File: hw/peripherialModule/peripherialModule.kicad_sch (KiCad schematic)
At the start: 20 parts, among them IC1 ATA6561-GAQW-N, J1 Conn_01x13_Socket, J2 Conn_01x13_Socket, J3 G17C0900132EU, J4 G17C0900132EU, J5 Conn_01x03_Socket, J6 726386-2, J7 726386-2, SW1 SW_Push, U1 TLV76133DCYR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

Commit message: boards are changing
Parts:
- removed J2: Conn_01x13_Socket, Connector_PinSocket_2.54mm:PinSocket_1x13_P2.54mm_Vertical, symbol Connector:Conn_01x13_Socket
- removed J6, J7: 726386-2, 726386-2, symbol FASTON:726386-2
- added J6, J9: Conn_01x03_Socket, Connector_PinSocket_2.54mm:PinSocket_1x03_P2.54mm_Vertical, symbol Connector:Conn_01x03_Socket
- added J8: Conn_01x05_Socket, Connector_PinSocket_2.54mm:PinSocket_1x05_P2.54mm_Vertical, symbol Connector:Conn_01x05_Socket
- J1: value Conn_01x13_Socket -> Conn_02x11_Socket; footprint Connector_PinSocket_2.54mm:PinSocket_1x13_P2.54mm_Vertical -> Connector_PinSocket_2.54mm:PinSocket_2x11_P2.54mm_Vertical; symbol Connector:Conn_01x13_Socket -> Connector_Generic:Conn_02x11_Odd_Even
- R2: value 100 -> 1k
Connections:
- net 24V: now also J9.1 (Pin_1), J9.2 (Pin_2), J9.3 (Pin_3)
- net 5.2V: now also J1.3 (Pin_3), J1.4 (Pin_4); no longer J1.1 (Pin_1), J1.2 (Pin_2)
- net GND: now also J1.1 (Pin_1), J1.2 (Pin_2), J6.1 (Pin_1), J6.2 (Pin_2), J6.3 (Pin_3), J8.3 (Pin_3); no longer J1.3 (Pin_3)
- net ICSP_CLK: now also J8.5 (Pin_5)
- net ICSP_DAT: now also J8.4 (Pin_4)
- net RA0: now also J1.8 (Pin_8); no longer J1.6 (Pin_6)
- net RA1: now also J1.10 (Pin_10); no longer J1.7 (Pin_7)
- net RA2: now also J1.12 (Pin_12); no longer J1.8 (Pin_8)
- net RA3: now also J1.14 (Pin_14); no longer J1.9 (Pin_9)
- net RA4: now also J1.16 (Pin_16); no longer J1.10 (Pin_10)
- net RA5: now also J1.18 (Pin_18); no longer J1.11 (Pin_11)
- net RA6: now also J1.20 (Pin_20); no longer J1.12 (Pin_12)
- net RA7: now also J1.22 (Pin_22); no longer J1.13 (Pin_13)
- net RC0: now also J1.15 (Pin_15)
- net RC1: now also J1.17 (Pin_17)
- net RC2: now also J1.19 (Pin_19)
- net RC3: now also J1.21 (Pin_21)
- net RC4: now also J1.13 (Pin_13)
- net RC5: now also J1.11 (Pin_11)
- net RC6: now also J1.9 (Pin_9)
- net RC7: now also J1.7 (Pin_7)
- net VDD: now also J1.6 (Pin_6), J8.2 (Pin_2); no longer J1.4 (Pin_4)
- net ~{MCLR}: now also J8.1 (Pin_1)

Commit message: hw - ledBoard
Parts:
- C4, C6: value 0.1u -> 0.1uF
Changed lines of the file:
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@@
       (effects (font (size 1.27 1.27)) (justify left))
     )
-    (property "Value" "0.1u" (at 194.31 132.08 0)
+    (property "Value" "0.1uF" (at 194.31 132.08 0)
       (effects (font (size 1.27 1.27)) (justify left))
     )
@@
       (effects (font (size 1.27 1.27)) (justify left))
     )
-    (property "Value" "0.1u" (at 273.05 90.17 0)
-      (effects (font (size 1.27 1.27)) (justify left))
-    )
+    (property "Value" "0.1uF" (at 273.05 90.17 0)
+      (effects (font (size 1.27 1.27)) (justify left))
+    )

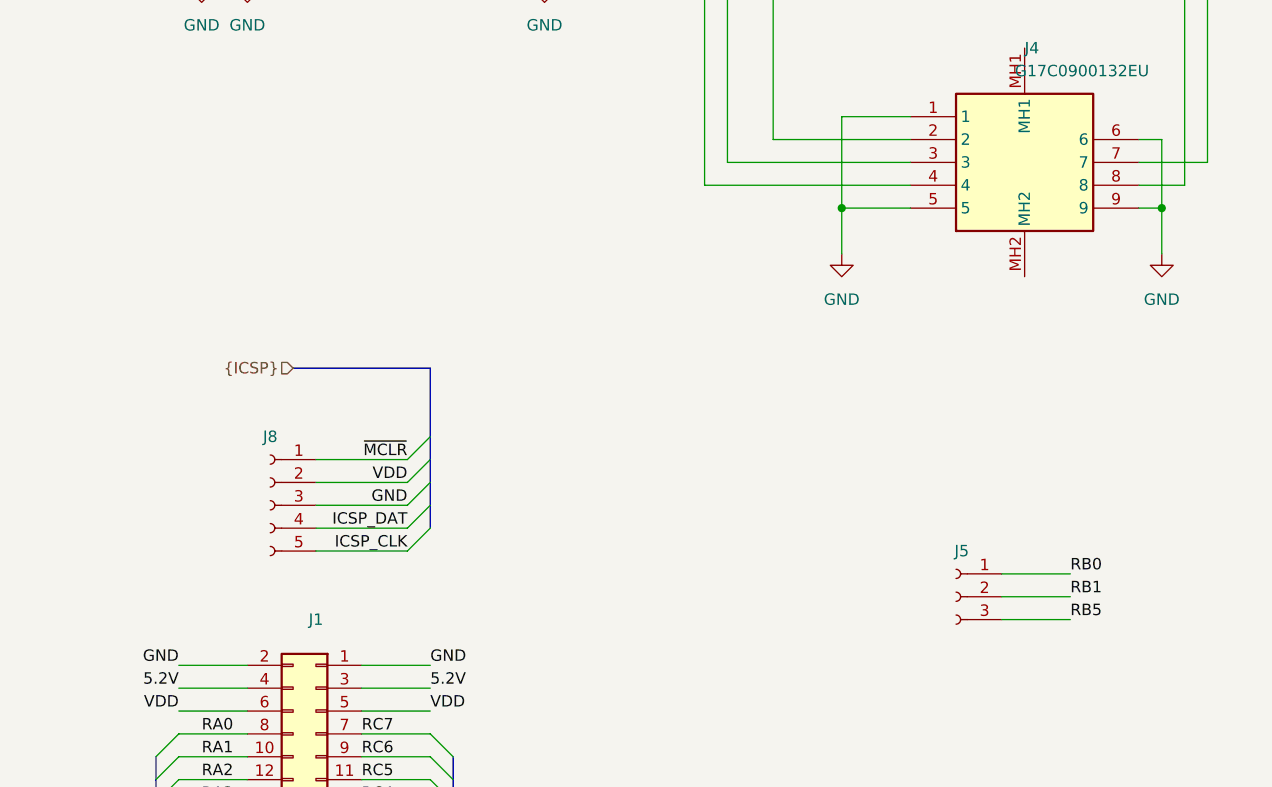
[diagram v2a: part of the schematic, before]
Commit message: text - periferie, obrazky hw - schemata
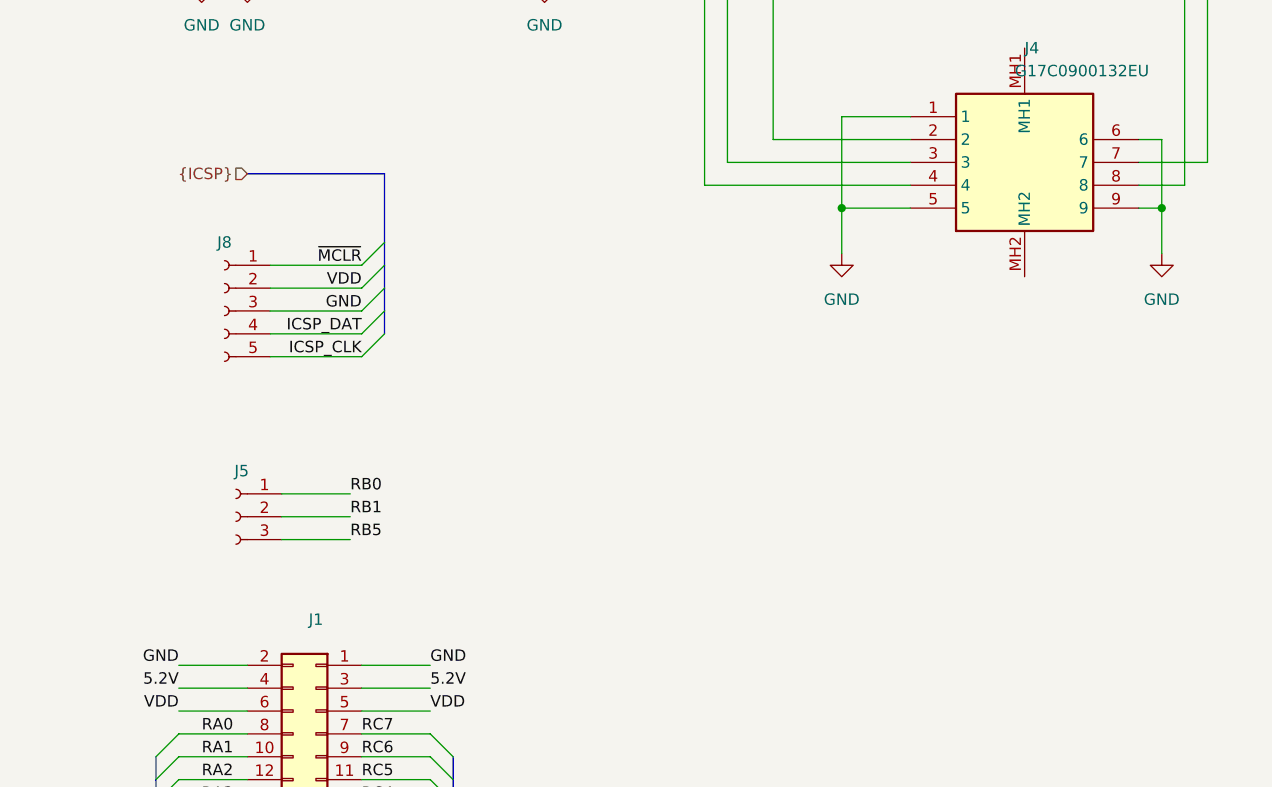
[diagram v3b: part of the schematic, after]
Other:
- moved on the sheet: J5, J8
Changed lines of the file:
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@@
     (stroke (width 0) (type default))
   )
-  (bus_entry (at 66.04 127) (size -2.54 2.54)
+  (bus_entry (at 60.96 105.41) (size -2.54 2.54)
     (stroke (width 0) (type default))
   )
@@
     (stroke (width 0) (type default))
   )
-  (bus_entry (at 66.04 137.16) (size -2.54 2.54)
+  (bus_entry (at 60.96 115.57) (size -2.54 2.54)
     (stroke (width 0) (type default))
   )
@@
     (stroke (width 0) (type default))
   )
-  (bus_entry (at 66.04 129.54) (size -2.54 2.54)
+  (bus_entry (at 60.96 107.95) (size -2.54 2.54)
     (stroke (width 0) (type default))
   )
@@
     (stroke (width 0) (type default))
   )
-  (bus_entry (at 66.04 134.62) (size -2.54 2.54)
+  (bus_entry (at 60.96 113.03) (size -2.54 2.54)
     (stroke (width 0) (type default))
   )
@@
     (stroke (width 0) (type default))
   )
-  (bus_entry (at 66.04 132.08) (size -2.54 2.54)
+  (bus_entry (at 60.96 110.49) (size -2.54 2.54)
     (stroke (width 0) (type default))
   )
@@
     (stroke (width 0) (type default))
   )
-  (wire (pts (xy 129.54 142.24) (xy 137.16 142.24))
+  (wire (pts (xy 49.53 133.35) (xy 57.15 133.35))
     (stroke (width 0) (type default))
   )
@@
     (stroke (width 0) (type default))
   )
-  (wire (pts (xy 63.5 139.7) (xy 53.34 139.7))
+  (wire (pts (xy 58.42 118.11) (xy 48.26 118.11))
     (stroke (width 0) (type default))
   )
@@
     (stroke (width 0) (type default))
   )
-  (bus (pts (xy 66.04 119.38) (xy 50.8 119.38))
+  (bus (pts (xy 60.96 97.79) (xy 45.72 97.79))
     (stroke (width 0) (type default))
   )
@@
     (stroke (width 0) (type default))
   )
-  (wire (pts (xy 129.54 147.32) (xy 137.16 147.32))
+  (wire (pts (xy 49.53 138.43) (xy 57.15 138.43))
     (stroke (width 0) (type default))
   )
@@
     (stroke (width 0) (type default))
   )
-  (wire (pts (xy 63.5 132.08) (xy 53.34 132.08))
+  (wire (pts (xy 58.42 110.49) (xy 48.26 110.49))
     (stroke (width 0) (type default))
   )
@@
     (stroke (width 0) (type default))
   )
-  (wire (pts (xy 129.54 144.78) (xy 137.16 144.78))
+  (wire (pts (xy 49.53 135.89) (xy 57.15 135.89))
     (stroke (width 0) (type default))
   )
@@
     (stroke (width 0) (type default))
   )
-  (bus (pts (xy 66.04 134.62) (xy 66.04 132.08))
+  (bus (pts (xy 60.96 113.03) (xy 60.96 110.49))
     (stroke (width 0) (type default))
   )
@@
     (stroke (width 0) (type default))
   )
-  (wire (pts (xy 63.5 137.16) (xy 53.34 137.16))
+  (wire (pts (xy 58.42 115.57) (xy 48.26 115.57))
     (stroke (width 0) (type default))
   )
@@
     (stroke (width 0) (type default))
   )
-  (bus (pts (xy 66.04 132.08) (xy 66.04 129.54))
+  (bus (pts (xy 60.96 110.49) (xy 60.96 107.95))
     (stroke (width 0) (type default))
   )
@@
     (stroke (width 0) (type default))
   )
-  (bus (pts (xy 66.04 129.54) (xy 66.04 127))
+  (bus (pts (xy 60.96 107.95) (xy 60.96 105.41))
     (stroke (width 0) (type default))
   )
@@
     (stroke (width 0) (type default))
   )
-  (bus (pts (xy 66.04 137.16) (xy 66.04 134.62))
+  (bus (pts (xy 60.96 115.57) (xy 60.96 113.03))
     (stroke (width 0) (type default))
   )
@@
     (stroke (width 0) (type default))
   )
-  (wire (pts (xy 63.5 129.54) (xy 53.34 129.54))
+  (wire (pts (xy 58.42 107.95) (xy 48.26 107.95))
     (stroke (width 0) (type default))
   )
@@
     (stroke (width 0) (type default))
   )
-  (bus (pts (xy 66.04 127) (xy 66.04 119.38))
+  (bus (pts (xy 60.96 105.41) (xy 60.96 97.79))
     (stroke (width 0) (type default))
   )
@@
     (stroke (width 0) (type default))
   )
-  (wire (pts (xy 63.5 134.62) (xy 53.34 134.62))
+  (wire (pts (xy 58.42 113.03) (xy 48.26 113.03))
     (stroke (width 0) (type default))
   )
@@
     (effects (font (size 1.27 1.27)) (justify left bottom))
   )
-  (label "RB0" (at 137.16 142.24 0) (fields_autoplaced)
+  (label "RB0" (at 57.15 133.35 0) (fields_autoplaced)
     (effects (font (size 1.27 1.27)) (justify left bottom))
   )
@@
     (effects (font (size 1.27 1.27)) (justify left bottom))
   )
-  (label "RB1" (at 137.16 144.78 0) (fields_autoplaced)
+  (label "RB1" (at 57.15 135.89 0) (fields_autoplaced)
     (effects (font (size 1.27 1.27)) (justify left bottom))
   )
@@
     (effects (font (size 1.27 1.27)) (justify left bottom))
   )
-  (label "ICSP_DAT" (at 63.5 137.16 180) (fields_autoplaced)
+  (label "ICSP_DAT" (at 58.42 115.57 180) (fields_autoplaced)
     (effects (font (size 1.27 1.27)) (justify right bottom))
   )
@@
     (effects (font (size 1.27 1.27)) (justify left bottom))
   )
-  (label "~{MCLR}" (at 63.5 129.54 180) (fields_autoplaced)
+  (label "~{MCLR}" (at 58.42 107.95 180) (fields_autoplaced)
     (effects (font (size 1.27 1.27)) (justify right bottom))
   )
-  (label "GND" (at 63.5 134.62 180) (fields_autoplaced)
+  (label "GND" (at 58.42 113.03 180) (fields_autoplaced)
     (effects (font (size 1.27 1.27)) (justify right bottom))
   )
@@
     (effects (font (size 1.27 1.27)) (justify left bottom))
   )
-  (label "RB5" (at 137.16 147.32 0) (fields_autoplaced)
+  (label "RB5" (at 57.15 138.43 0) (fields_autoplaced)
     (effects (font (size 1.27 1.27)) (justify left bottom))
   )
@@
     (effects (font (size 1.27 1.27)) (justify left bottom))
   )
-  (label "VDD" (at 63.5 132.08 180) (fields_autoplaced)
+  (label "VDD" (at 58.42 110.49 180) (fields_autoplaced)
     (effects (font (size 1.27 1.27)) (justify right bottom))
   )
@@
     (effects (font (size 1.27 1.27)) (justify left bottom))
   )
-  (label "ICSP_CLK" (at 63.5 139.7 180) (fields_autoplaced)
+  (label "ICSP_CLK" (at 58.42 118.11 180) (fields_autoplaced)
     (effects (font (size 1.27 1.27)) (justify right bottom))
   )
@@
     (effects (font (size 1.27 1.27)) (justify left))
   )
-  (hierarchical_label "{ICSP}" (shape input) (at 50.8 119.38 180) (fields_autoplaced)
+  (hierarchical_label "{ICSP}" (shape input) (at 45.72 97.79 180) (fields_autoplaced)
     (effects (font (size 1.27 1.27)) (justify right))
   )
@@
     )
   )
-  (symbol (lib_id "Connector:Conn_01x03_Socket") (at 124.46 144.78 0) (mirror y) (unit 1)
-    (in_bom yes) (on_board yes) (dnp no) (fields_autoplaced)
-    (property "Reference" "J5" (at 125.095 139.7 0)
-      (effects (font (size 1.27 1.27)))
-    )
-    (property "Value" "Conn_01x03_Socket" (at 125.095 139.7 0)
-      (effects (font (size 1.27 1.27)) hide)
-    )
-    (property "Footprint" "Connector_PinSocket_2.54mm:PinSocket_1x03_P2.54mm_Vertical" (at 124.46 144.78 0)
-      (effects (font (size 1.27 1.27)) hide)
-    )
-    (property "Datasheet" "~" (at 124.46 144.78 0)
+  (symbol (lib_id "Connector:Conn_01x03_Socket") (at 44.45 135.89 0) (mirror y) (unit 1)
+    (in_bom yes) (on_board yes) (dnp no) (fields_autoplaced)
+    (property "Reference" "J5" (at 45.085 130.81 0)
+      (effects (font (size 1.27 1.27)))
+    )
+    (property "Value" "Conn_01x03_Socket" (at 45.085 130.81 0)
+      (effects (font (size 1.27 1.27)) hide)
+    )
+    (property "Footprint" "Connector_PinSocket_2.54mm:PinSocket_1x03_P2.54mm_Vertical" (at 44.45 135.89 0)
+      (effects (font (size 1.27 1.27)) hide)
+    )
+    (property "Datasheet" "~" (at 44.45 135.89 0)
       (effects (font (size 1.27 1.27)) hide)
     )
@@
     )
   )
-  (symbol (lib_id "Connector:Conn_01x05_Socket") (at 48.26 134.62 0) (mirror y) (unit 1)
+  (symbol (lib_id "Connector:Conn_01x05_Socket") (at 43.18 113.03 0) (mirror y) (unit 1)
     (in_bom yes) (on_board yes) (dnp no)
-    (property "Reference" "J8" (at 48.26 127 0)
-      (effects (font (size 1.27 1.27)))
-    )
-    (property "Value" "Conn_01x05_Socket" (at 53.34 114.3 0)
-      (effects (font (size 1.27 1.27)) hide)
-    )
-    (property "Footprint" "Connector_PinSocket_2.54mm:PinSocket_1x05_P2.54mm_Vertical" (at 48.26 134.62 0)
-      (effects (font (size 1.27 1.27)) hide)
-    )
-    (property "Datasheet" "~" (at 48.26 134.62 0)
-      (effects (font (size 1.27 1.27)) hide)
-    )
+    (property "Reference" "J8" (at 43.18 105.41 0)
+      (effects (font (size 1.27 1.27)))
+    )
+    (property "Value" "Conn_01x05_Socket" (at 48.26 92.71 0)
+      (effects (font (size 1.27 1.27)) hide)
+    )
+    (property "Footprint" "Connector_PinSocket_2.54mm:PinSocket_1x05_P2.54mm_Vertical" (at 43.18 113.03 0)
+      (effects (font (size 1.27 1.27)) hide)
+    )
+    (property "Datasheet" "~" (at 43.18 113.03 0)
+      (effects (font (size 1.27 1.27)) hide)
+    )
